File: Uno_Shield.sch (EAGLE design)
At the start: 21 parts, among them IC1 MPL3115A2LGA, U1 USD-SOCKETNEW, U2 74HC4050, U4 FGPMMOPA6H, X1 22-23-2021

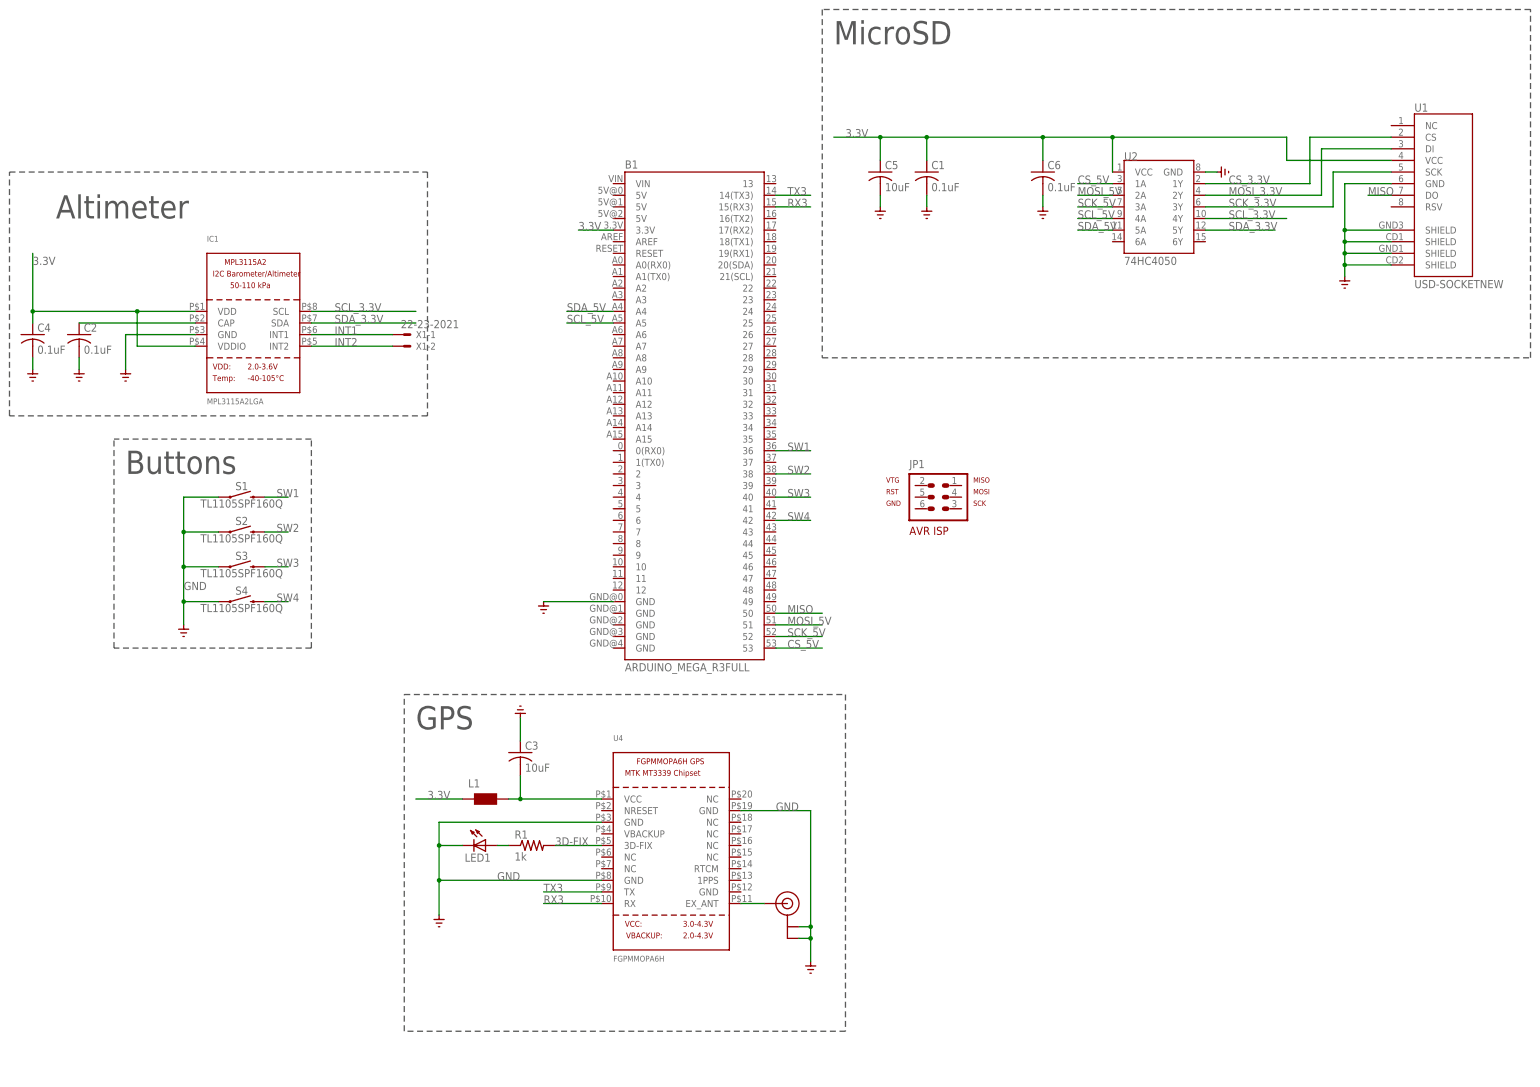
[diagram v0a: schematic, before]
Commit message: Rev 0.2
Uno edition
Mega edition

Individual switches (cheaper, replacable!)
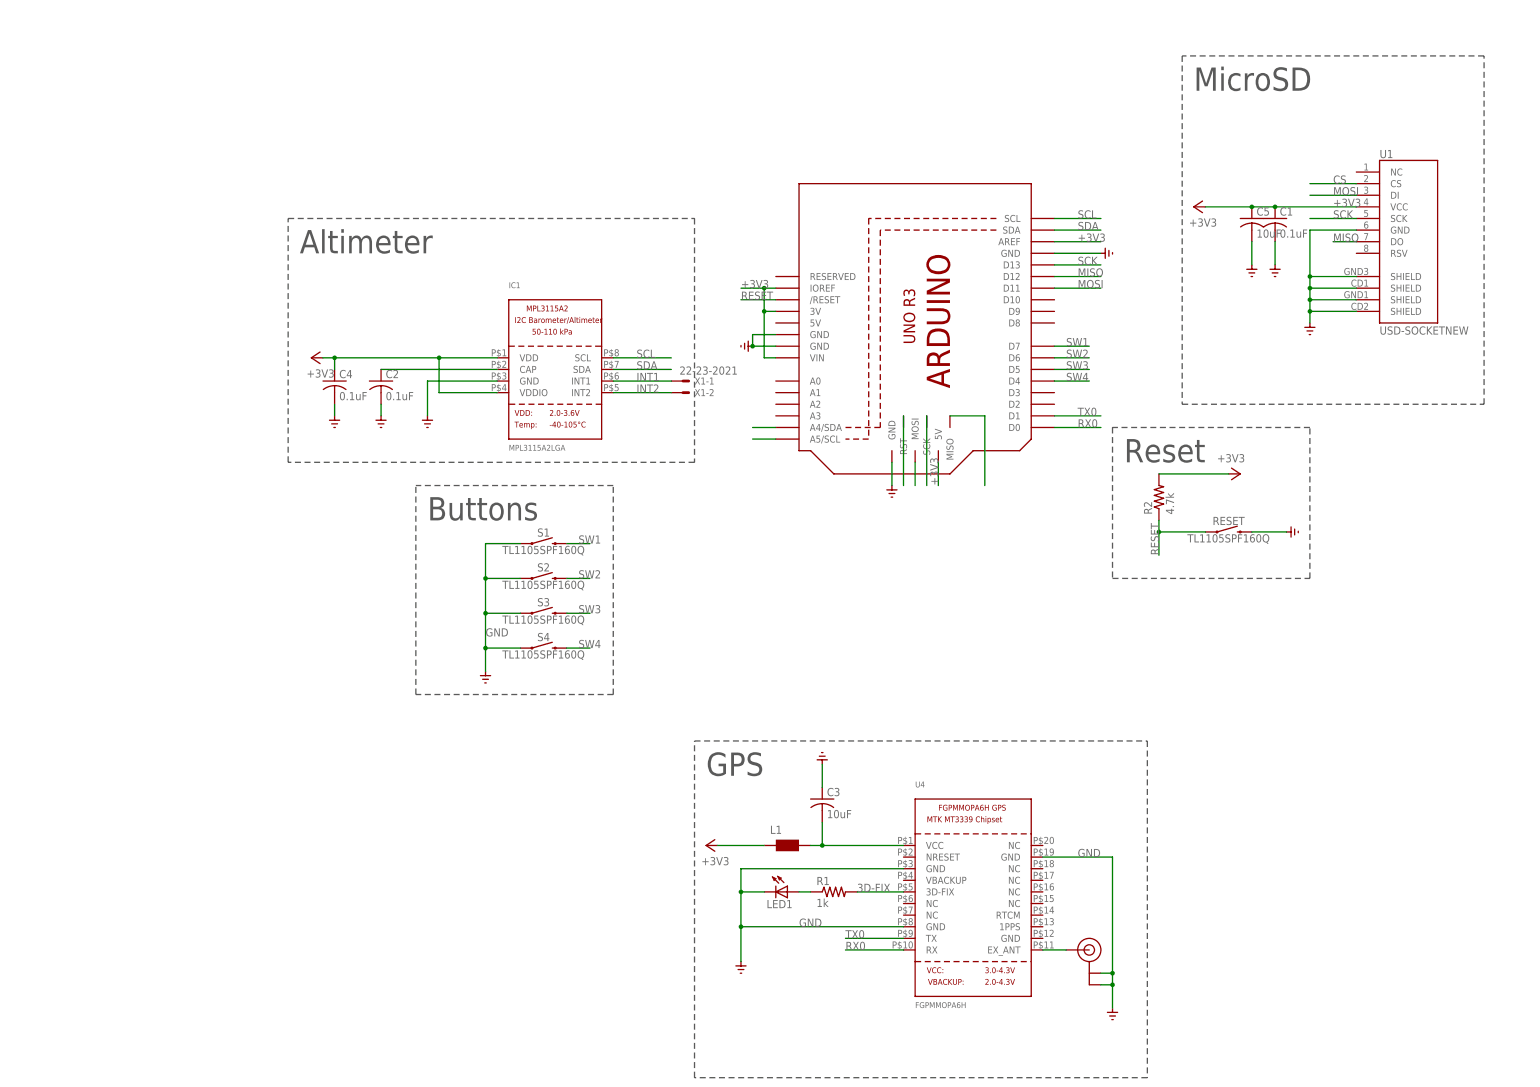
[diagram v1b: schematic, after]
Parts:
- removed B1: ARDUINO_MEGA_R3FULL, SparkFun-Boards:ARDUINO_MEGA_R3FULL
- removed C6: 0.1uF, adafruit:C-USC1206
- removed JP1: AVR-ISP-6, atmel-1:AVR-ISP-6
- removed U2: 74HC4050, SparkFun-IC-Comms:HEX_CONVERTER
- added M1: ARDUINO_R3_ICSP, adafruit:ARDUINO_R3_ICSP
- added R2: 4.7k, adafruit:R-US_R1206
- added RESET: TL1105SPF160Q, SparkFun-Switches:MOMENTARY-SWITCH-SPST-PTH-6.0MM
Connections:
- removed net 3.3V: B1.3.3V, C1.1, C4.1, C5.1, C6.1, IC1.VDD, IC1.VDDIO, L1.1, U1.VCC, U2.VCC
- removed net CS_3.3V: U1.CS, U2.1Y
- removed net CS_5V: B1.53, U2.1A
- removed net MOSI_3.3V: U1.DI, U2.2Y
- removed net MOSI_5V: B1.51, U2.2A
- removed net RX3: B1.15(RX3), U4.RX
- removed net SCK_3.3V: U1.SCK, U2.3Y
- removed net SCK_5V: B1.52, U2.3A
- removed net SCL_3.3V: IC1.SCL, U2.4Y
- removed net SCL_5V: B1.A5, U2.4A
- removed net SDA_3.3V: IC1.SDA, U2.5Y
- removed net SDA_5V: B1.A4, U2.5A
- removed net TX3: B1.14(TX3), U4.TX
- new net +3V3: C1.1, C4.1, C5.1, IC1.VDD, IC1.VDDIO, L1.1, M1.3V, M1.5V@1, M1.AREF, M1.IOREF, M1.VIN, R2.2, U1.VCC
- new net CS: U1.CS
- new net MOSI: M1.D11, M1.MOSI, U1.DI
- new net RESET: M1./RESET, M1.RST, R2.1, RESET.1
- new net RX0: M1.D0, U4.RX
- new net SCK: M1.D13, M1.SCK, U1.SCK
- new net SCL: IC1.SCL, M1.A5/SCL, M1.SCL
- new net SDA: IC1.SDA, M1.A4/SDA, M1.SDA
- new net TX0: M1.D1, U4.TX
- net GND: now also M1.GND, M1.GND@1, M1.GND@2, M1.GND@3, RESET.2; no longer B1.GND@0, C6.2, U2.GND
- net MISO: now also M1.D12, M1.MISO; no longer B1.50
- net SW1: now also M1.D7; no longer B1.36
- net SW2: now also M1.D6; no longer B1.38
- net SW3: now also M1.D5; no longer B1.40
- net SW4: now also M1.D4; no longer B1.42
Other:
- note added: "Reset"
- moved on the sheet: C1, C2, C3, C4, C5, IC1, L1, LED1, R1, S1, S2, S3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
